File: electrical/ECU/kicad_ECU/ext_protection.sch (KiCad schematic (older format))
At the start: 8 parts

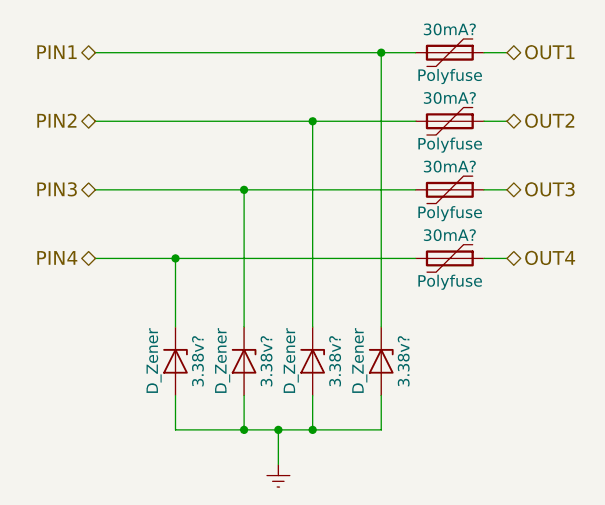
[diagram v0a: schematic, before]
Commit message: fixed some naming errors and initial round of double checking
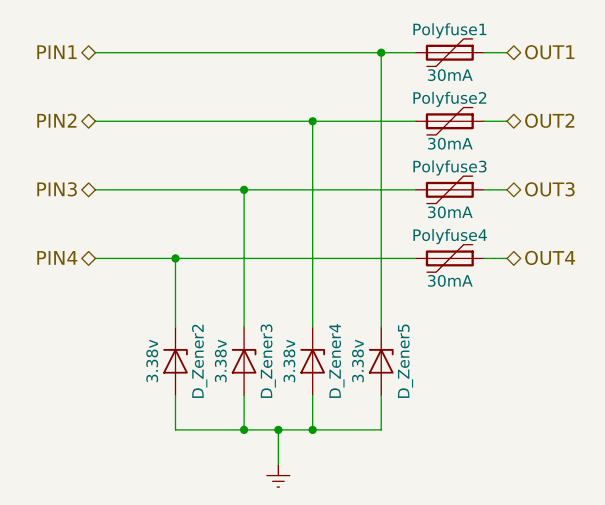
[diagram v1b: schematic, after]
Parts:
- removed 3.38v? (x3): D_Zener, symbol D_Zener
- removed 30mA? (x3): Polyfuse, symbol Polyfuse
- added D_Zener3, D_Zener4, D_Zener5: 3.38v, symbol D_Zener
- added Polyfuse2, Polyfuse3, Polyfuse4: 30mA, symbol Polyfuse
- D_Zener2: renamed from 3.38v?; value D_Zener -> 3.38v
- Polyfuse1: renamed from 30mA?; value Polyfuse -> 30mA
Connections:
- net Earth: now also D_Zener3.2 (A), D_Zener4.2 (A), D_Zener5.2 (A)
- net OUT2: now also Polyfuse2.1
- net OUT3: now also Polyfuse3.1
- net OUT4: now also Polyfuse4.1
- net PIN1: now also D_Zener5.1 (K)
- net PIN2: now also D_Zener4.1 (K), Polyfuse2.2
- net PIN3: now also D_Zener3.1 (K), Polyfuse3.2
- net PIN4: now also Polyfuse4.2
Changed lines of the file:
@@
 $Descr A4 11693 8268
 encoding utf-8
-Sheet 29 33
+Sheet 31 33
 Title "External pin protection"
 Date ""
@@
 OUT1
 $Comp
-L Polyfuse 30mA?
+L Polyfuse Polyfuse1
 U 1 1 597FE5B1
 P 6400 2550
-F 0 "30mA?" V 6300 2550 50  0000 C CNN
-F 1 "Polyfuse" V 6500 2550 50  0000 C CNN
+F 0 "Polyfuse1" V 6300 2550 50  0000 C CNN
+F 1 "30mA" V 6500 2550 50  0000 C CNN
 F 2 "" H 6450 2350 50  0001 L CNN
 F 3 "" H 6400 2550 50  0001 C CNN
@@
 	4850 2550 6250 2550
 $Comp
-L D_Zener 3.38v?
+L D_Zener D_Zener2
 U 1 1 597FE5BA
 P 5200 3900
-F 0 "3.38v?" H 5200 4000 50  0000 C CNN
-F 1 "D_Zener" H 5200 3800 50  0000 C CNN
+F 0 "D_Zener2" H 5200 4000 50  0000 C CNN
+F 1 "3.38v" H 5200 3800 50  0000 C CNN
 F 2 "" H 5200 3900 50  0001 C CNN
 F 3 "" H 5200 3900 50  0001 C CNN
@@
 Text HLabel 6650 2850 2    60   BiDi ~ 0
 OUT2
-$Comp
-L Polyfuse 30mA?
-U 1 1 597FE5C5
-P 6400 2850
-F 0 "30mA?" V 6300 2850 50  0000 C CNN
-F 1 "Polyfuse" V 6500 2850 50  0000 C CNN
-F 2 "" H 6450 2650 50  0001 L CNN
-F 3 "" H 6400 2850 50  0001 C CNN
-	1    6400 2850
-	0    1    1    0
-$EndComp
 Wire Wire Line
 	4850 2850 6250 2850
-$Comp
-L D_Zener 3.38v?
-U 1 1 597FE5CE
-P 5500 3900
-F 0 "3.38v?" H 5500 4000 50  0000 C CNN
-F 1 "D_Zener" H 5500 3800 50  0000 C CNN
-F 2 "" H 5500 3900 50  0001 C CNN
-F 3 "" H 5500 3900 50  0001 C CNN
-	1    5500 3900
-	0    1    1    0
-$EndComp
 Wire Wire Line
 	6550 2850 6650 2850
@@
 Text HLabel 6650 3150 2    60   BiDi ~ 0
 OUT3
-$Comp
-L Polyfuse 30mA?
-U 1 1 597FE5D9
-P 6400 3150
-F 0 "30mA?" V 6300 3150 50  0000 C CNN
-F 1 "Polyfuse" V 6500 3150 50  0000 C CNN
-F 2 "" H 6450 2950 50  0001 L CNN
-F 3 "" H 6400 3150 50  0001 C CNN
-	1    6400 3150
-	0    1    1    0
-$EndComp
 Wire Wire Line
 	4850 3150 6250 3150
 $Comp
-L D_Zener 3.38v?
-U 1 1 597FE5E2
-P 5800 3900
-F 0 "3.38v?" H 5800 4000 50  0000 C CNN
-F 1 "D_Zener" H 5800 3800 50  0000 C CNN
-F 2 "" H 5800 3900 50  0001 C CNN
-F 3 "" H 5800 3900 50  0001 C CNN
-	1    5800 3900
-	0    1    1    0
-$EndComp
-$Comp
-L Earth #PWR?
+L Earth #PWR68
 U 1 1 597FE5E9
 P 5650 4350
-F 0 "#PWR?" H 5650 4100 50  0001 C CNN
+F 0 "#PWR68" H 5650 4100 50  0001 C CNN
 F 1 "Earth" H 5650 4200 50  0001 C CNN
 F 2 "" H 5650 4350 50  0001 C CNN
@@
 Text HLabel 6650 3450 2    60   BiDi ~ 0
 OUT4
-$Comp
-L Polyfuse 30mA?
-U 1 1 597FE5F3
-P 6400 3450
-F 0 "30mA?" V 6300 3450 50  0000 C CNN
-F 1 "Polyfuse" V 6500 3450 50  0000 C CNN
-F 2 "" H 6450 3250 50  0001 L CNN
-F 3 "" H 6400 3450 50  0001 C CNN
-	1    6400 3450
-	0    1    1    0
-$EndComp
 Wire Wire Line
 	4850 3450 6250 3450
-$Comp
-L D_Zener 3.38v?
-U 1 1 597FE5FC
-P 6100 3900
-F 0 "3.38v?" H 6100 4000 50  0000 C CNN
-F 1 "D_Zener" H 6100 3800 50  0000 C CNN
-F 2 "" H 6100 3900 50  0001 C CNN
-F 3 "" H 6100 3900 50  0001 C CNN
-	1    6100 3900
-	0    1    1    0
-$EndComp
 Wire Wire Line
 	6550 3450 6650 3450
@@
 Text HLabel 4850 3450 0    60   BiDi ~ 0
 PIN4
+$Comp
+L Polyfuse Polyfuse2
+U 1 1 59961BEE
+P 6400 2850
+F 0 "Polyfuse2" V 6300 2850 50  0000 C CNN
+F 1 "30mA" V 6500 2850 50  0000 C CNN
+F 2 "" H 6450 2650 50  0001 L CNN
+F 3 "" H 6400 2850 50  0001 C CNN
+	1    6400 2850
+	0    1    1    0
+$EndComp
+$Comp
+L Polyfuse Polyfuse3
+U 1 1 59961C1E
+P 6400 3150
+F 0 "Polyfuse3" V 6300 3150 50  0000 C CNN
+F 1 "30mA" V 6500 3150 50  0000 C CNN
+F 2 "" H 6450 2950 50  0001 L CNN
+F 3 "" H 6400 3150 50  0001 C CNN
+	1    6400 3150
+	0    1    1    0
+$EndComp
+$Comp
+L Polyfuse Polyfuse4
+U 1 1 59961C53
+P 6400 3450
+F 0 "Polyfuse4" V 6300 3450 50  0000 C CNN
+F 1 "30mA" V 6500 3450 50  0000 C CNN
+F 2 "" H 6450 3250 50  0001 L CNN
+F 3 "" H 6400 3450 50  0001 C CNN
+	1    6400 3450
+	0    1    1    0
+$EndComp
+$Comp
+L D_Zener D_Zener3
+U 1 1 59961CCE
+P 5500 3900
+F 0 "D_Zener3" H 5500 4000 50  0000 C CNN
+F 1 "3.38v" H 5500 3800 50  0000 C CNN
+F 2 "" H 5500 3900 50  0001 C CNN
+F 3 "" H 5500 3900 50  0001 C CNN
+	1    5500 3900
+	0    1    1    0
+$EndComp
+$Comp
+L D_Zener D_Zener4
+U 1 1 59961CF9
+P 5800 3900
+F 0 "D_Zener4" H 5800 4000 50  0000 C CNN
+F 1 "3.38v" H 5800 3800 50  0000 C CNN
+F 2 "" H 5800 3900 50  0001 C CNN
+F 3 "" H 5800 3900 50  0001 C CNN
+	1    5800 3900
+	0    1    1    0
+$EndComp
+$Comp
+L D_Zener D_Zener5
+U 1 1 59961D22
+P 6100 3900
+F 0 "D_Zener5" H 6100 4000 50  0000 C CNN
+F 1 "3.38v" H 6100 3800 50  0000 C CNN
+F 2 "" H 6100 3900 50  0001 C CNN
+F 3 "" H 6100 3900 50  0001 C CNN
+	1    6100 3900
+	0    1    1    0
+$EndComp
 $EndSCHEMATC
